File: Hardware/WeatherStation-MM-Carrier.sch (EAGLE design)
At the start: 87 parts, among them J11 microSD, J13 RJ11 - WIND, J15 MICROMOD-2222-C, J2 JTAG, J3 QWIIC_RIGHT_ANGLE, J7 RJ11 - RAIN, U1 BME280, U2 VEML6075, U3 AS3935, U5 AP7361C-33FGEUDFN-8

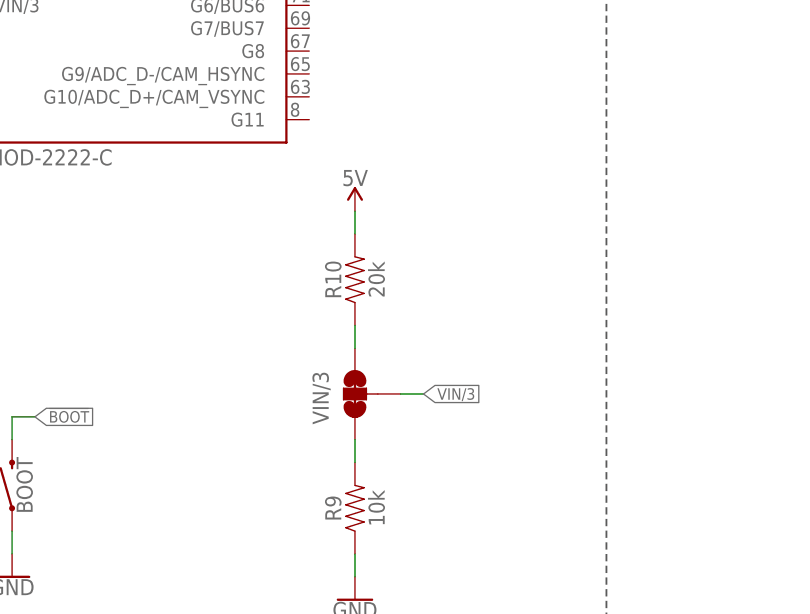
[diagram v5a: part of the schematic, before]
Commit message: Removed VIN/3 jumper
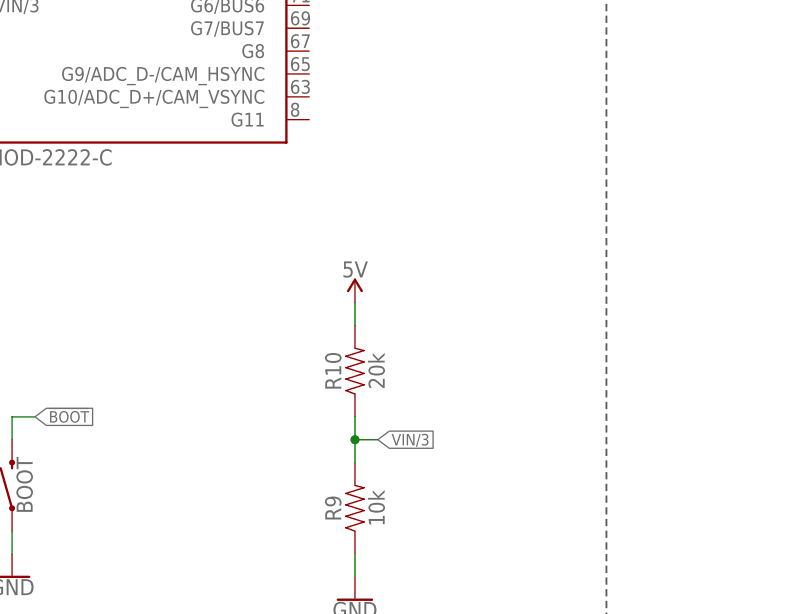
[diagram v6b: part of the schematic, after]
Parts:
- removed JP5: VIN/3, SparkFun-Jumpers:JUMPER-SMT_3_2-NC_TRACE_SILK
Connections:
- removed net N$12: JP5.1, R9.2
- removed net N$9: JP5.3, R10.1
- net VIN/3: now also R10.1, R9.2; no longer JP5.2
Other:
- moved on the sheet: R10
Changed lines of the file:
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@@
 <part name="LOGO1" library="SparkFun-Aesthetics" deviceset="SFE_LOGO_NAME_FLAME" device=".2_INCH"/>
 <part name="JP3" library="SparkFun-Jumpers" deviceset="JUMPER-SMT_2_NC_TRACE" device="_SILK" package3d_urn="urn:adsk.eagle:package:39281/1" value="UV"/>
-<part name="JP5" library="SparkFun-Jumpers" deviceset="JUMPER-SMT_3_2-NC_TRACE" device="_SILK" package3d_urn="urn:adsk.eagle:package:39289/1" value="VIN/3"/>
 <part name="JP6" library="SparkFun-Jumpers" deviceset="JUMPER-SMT_2_NO" device="_SILK" package3d_urn="urn:adsk.eagle:package:39279/1" value="VE"/>
 </parts>
@@
 <attribute name="VALUE" x="141.224" y="15.24" size="1.778" layer="96" font="vector" rot="R90" align="top-center"/>
 </instance>
-<instance part="R10" gate="G$1" x="139.7" y="40.64" smashed="yes" rot="R90">
-<attribute name="NAME" x="138.176" y="40.64" size="1.778" layer="95" font="vector" rot="R90" align="bottom-center"/>
-<attribute name="VALUE" x="141.224" y="40.64" size="1.778" layer="96" font="vector" rot="R90" align="top-center"/>
+<instance part="R10" gate="G$1" x="139.7" y="30.48" smashed="yes" rot="R90">
+<attribute name="NAME" x="138.176" y="30.48" size="1.778" layer="95" font="vector" rot="R90" align="bottom-center"/>
+<attribute name="VALUE" x="141.224" y="30.48" size="1.778" layer="96" font="vector" rot="R90" align="top-center"/>
 </instance>
 <instance part="GND11" gate="1" x="139.7" y="5.08" smashed="yes">
@@
 <attribute name="VALUE" x="83.82" y="211.074" size="1.778" layer="96" align="bottom-center"/>
 </instance>
-<instance part="SUPPLY19" gate="G$1" x="139.7" y="48.26" smashed="yes">
-<attribute name="VALUE" x="139.7" y="51.054" size="1.778" layer="96" align="bottom-center"/>
+<instance part="SUPPLY19" gate="G$1" x="139.7" y="38.1" smashed="yes">
+<attribute name="VALUE" x="139.7" y="40.894" size="1.778" layer="96" align="bottom-center"/>
 </instance>
 <instance part="MEAS" gate="JP1" x="106.68" y="259.08" smashed="yes">
@@
 <instance part="JP3" gate="G$1" x="381" y="256.54" smashed="yes" rot="R90">
 <attribute name="VALUE" x="383.54" y="255.016" size="1.778" layer="96" font="vector" rot="R90" align="top-left"/>
-</instance>
-<instance part="JP5" gate="G$1" x="139.7" y="27.94" smashed="yes" rot="R180">
-<attribute name="VALUE" x="136.779" y="30.48" size="1.778" layer="96" font="vector" rot="R270" align="top-left"/>
 </instance>
 <instance part="JP6" gate="G$1" x="35.56" y="241.3" smashed="yes" rot="R90">
@@
 <pinref part="R10" gate="G$1" pin="2"/>
 <pinref part="SUPPLY19" gate="G$1" pin="5V"/>
-<wire x1="139.7" y1="48.26" x2="139.7" y2="45.72" width="0.1524" layer="91"/>
+<wire x1="139.7" y1="38.1" x2="139.7" y2="35.56" width="0.1524" layer="91"/>
 </segment>
 <segment>
@@
 </segment>
 <segment>
-<pinref part="JP5" gate="G$1" pin="2"/>
-<wire x1="144.78" y1="27.94" x2="147.32" y2="27.94" width="0.1524" layer="91"/>
-<label x="147.32" y="27.94" size="1.27" layer="95" xref="yes"/>
+<pinref part="R9" gate="G$1" pin="2"/>
+<pinref part="R10" gate="G$1" pin="1"/>
+<wire x1="139.7" y1="20.32" x2="139.7" y2="22.86" width="0.1524" layer="91"/>
+<wire x1="139.7" y1="22.86" x2="139.7" y2="25.4" width="0.1524" layer="91"/>
+<wire x1="139.7" y1="22.86" x2="142.24" y2="22.86" width="0.1524" layer="91"/>
+<junction x="139.7" y="22.86"/>
+<label x="142.24" y="22.86" size="1.27" layer="95" xref="yes"/>
 </segment>
 </net>
@@
 </segment>
 </net>
-<net name="N$9" class="0">
-<segment>
-<pinref part="JP5" gate="G$1" pin="3"/>
-<pinref part="R10" gate="G$1" pin="1"/>
-<wire x1="139.7" y1="33.02" x2="139.7" y2="35.56" width="0.1524" layer="91"/>
-</segment>
-</net>
-<net name="N$12" class="0">
-<segment>
-<pinref part="R9" gate="G$1" pin="2"/>
-<pinref part="JP5" gate="G$1" pin="1"/>
-<wire x1="139.7" y1="20.32" x2="139.7" y2="22.86" width="0.1524" layer="91"/>
-</segment>
-</net>

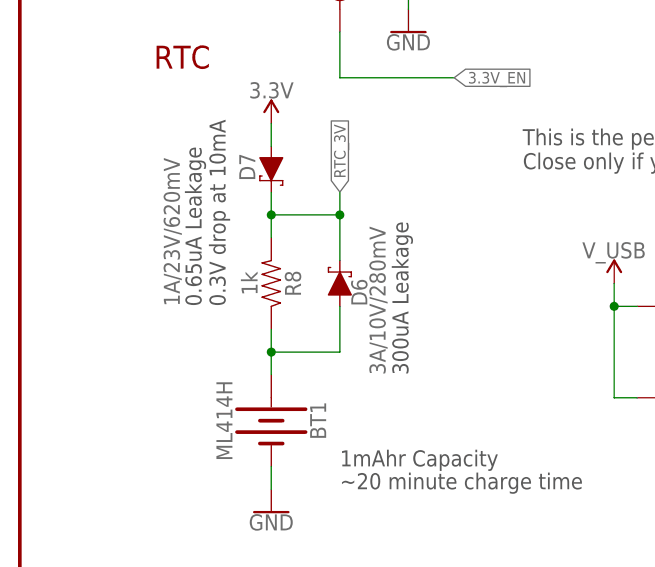
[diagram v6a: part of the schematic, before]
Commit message: Moved silkscreen
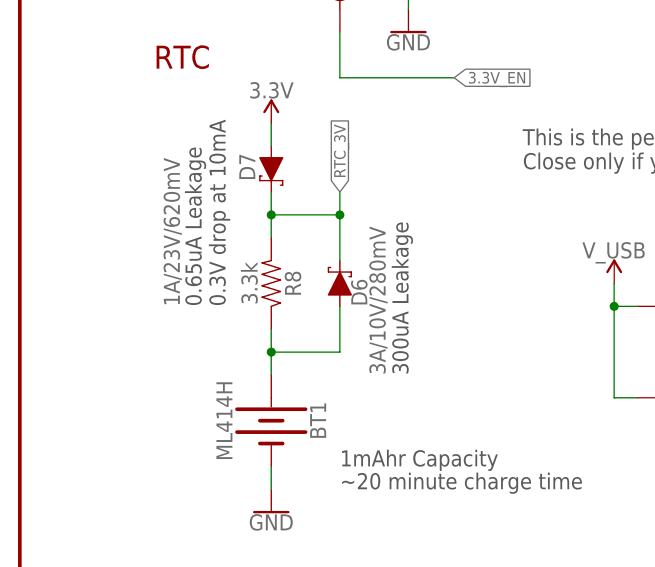
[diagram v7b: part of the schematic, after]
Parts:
- R8: value 1k -> 3.3k; device SparkFun-Resistors:1KOHM-0603-1/10W-1% -> SparkFun-Resistors:3.3KOHM-0603-1/10W-1%
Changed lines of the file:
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@@
 <part name="BT1" library="SparkFun-Batteries" deviceset="ML414H_IV01E_BATTERY" device="" value="ML414H"/>
 <part name="D6" library="SparkFun-DiscreteSemi" deviceset="DIODE-SCHOTTKY" device="-BAT60A" value="3A/10V/280mV"/>
-<part name="R8" library="SparkFun-Resistors" deviceset="1KOHM" device="-0603-1/10W-1%" value="1k"/>
+<part name="R8" library="SparkFun-Resistors" deviceset="3.3KOHM" device="-0603-1/10W-1%" value="3.3k"/>
 <part name="GND51" library="SparkFun-PowerSymbols" deviceset="GND" device=""/>
 <part name="SUPPLY26" library="SparkFun-PowerSymbols" deviceset="3.3V" device=""/>

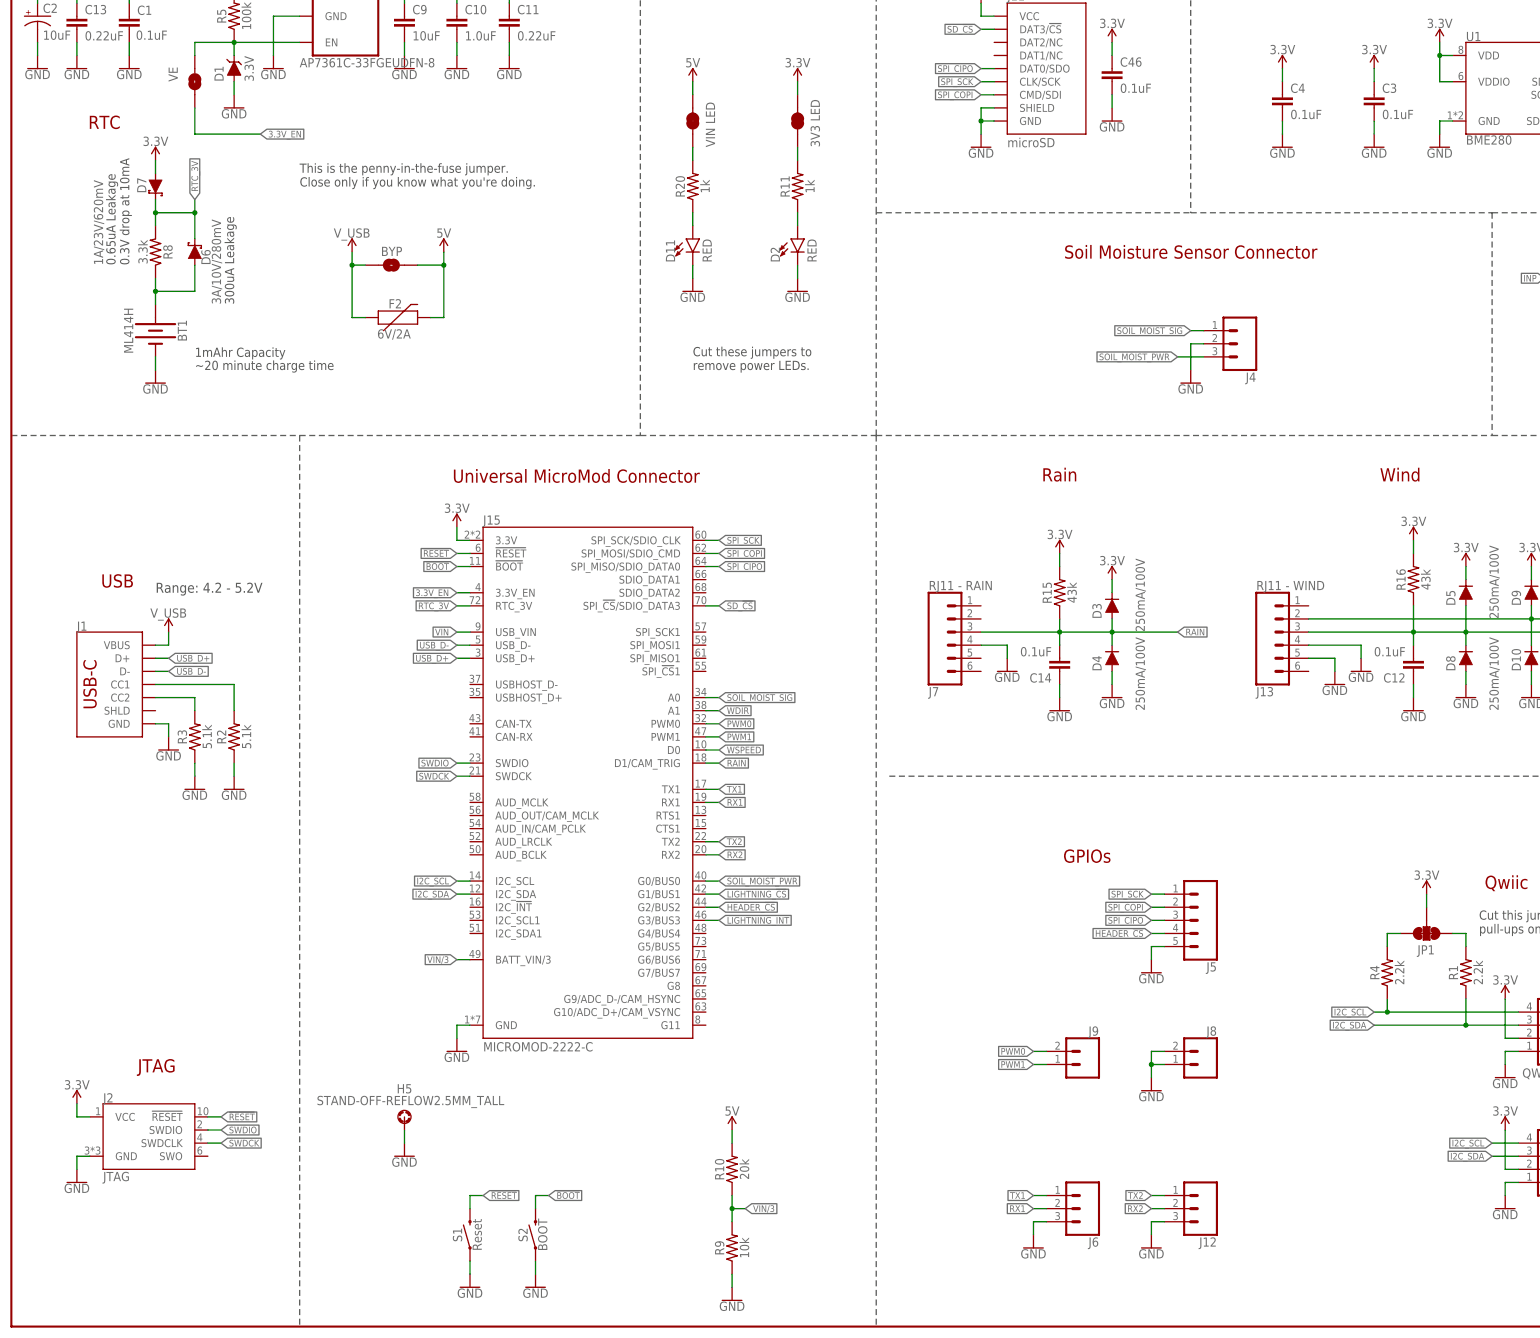
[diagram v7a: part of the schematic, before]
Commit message: QC Double check changes
Added SWDIO test point, notes on VE jumper, measurements for standoffs, double check sparkle BOM, and DRC
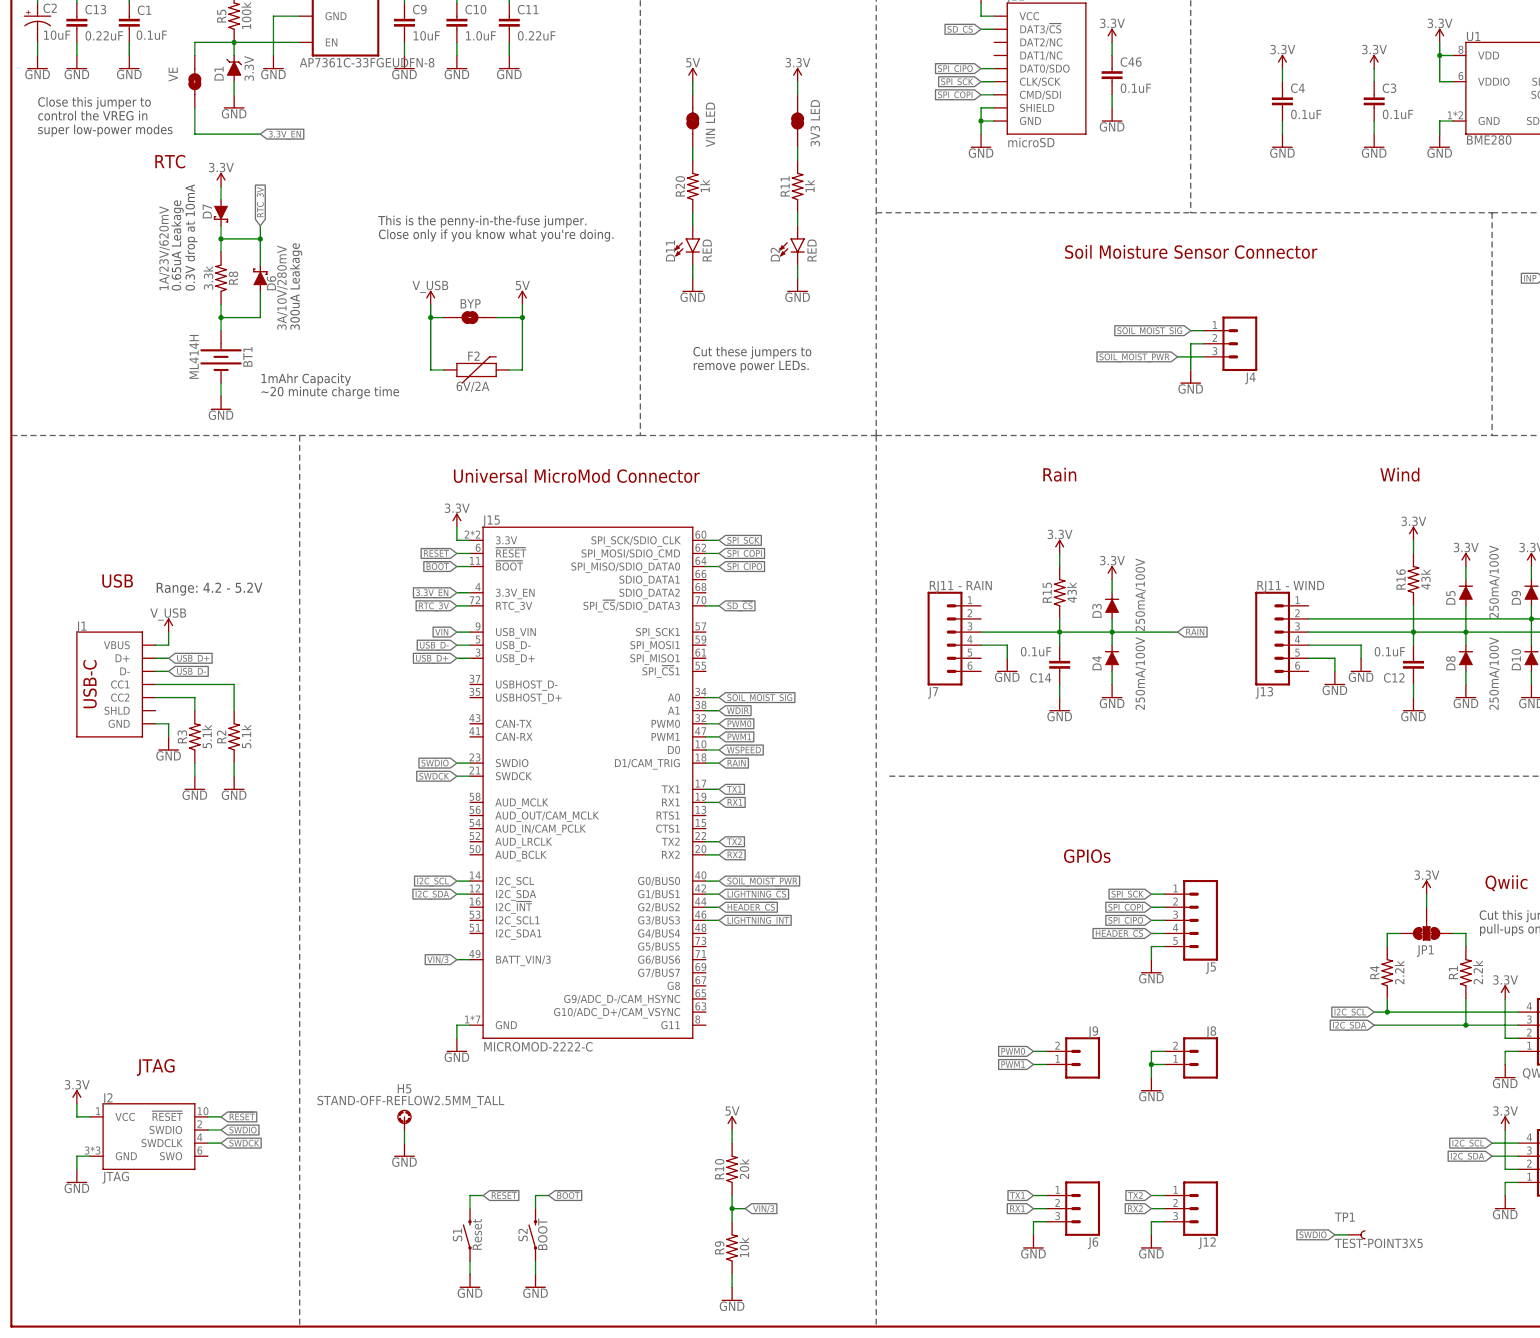
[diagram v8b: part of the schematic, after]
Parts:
- added TP1: TEST-POINT3X5, SparkFun-Connectors:TEST-POINT3X5
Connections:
- net SWDIO: now also TP1.1
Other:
- note added: "Close this jumper to control the VREG in super low-power modes"
- moved on the sheet: BT1, BYP, D6, D7, F2, R8
